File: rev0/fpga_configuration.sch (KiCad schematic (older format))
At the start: 23 parts, among them IC1 ECP5-BGA256, U5 ATSAMD21G18A-AUT, U6 W25Q32JVSS

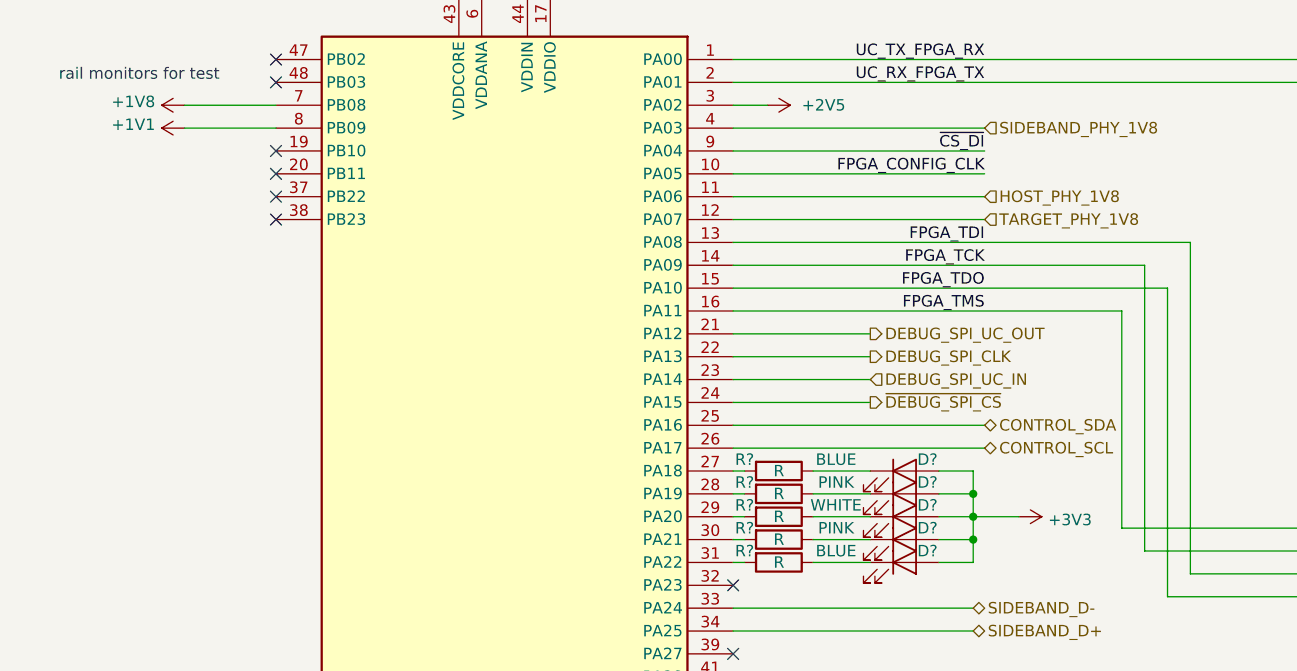
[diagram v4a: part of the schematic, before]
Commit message: schematic: finish initial capture
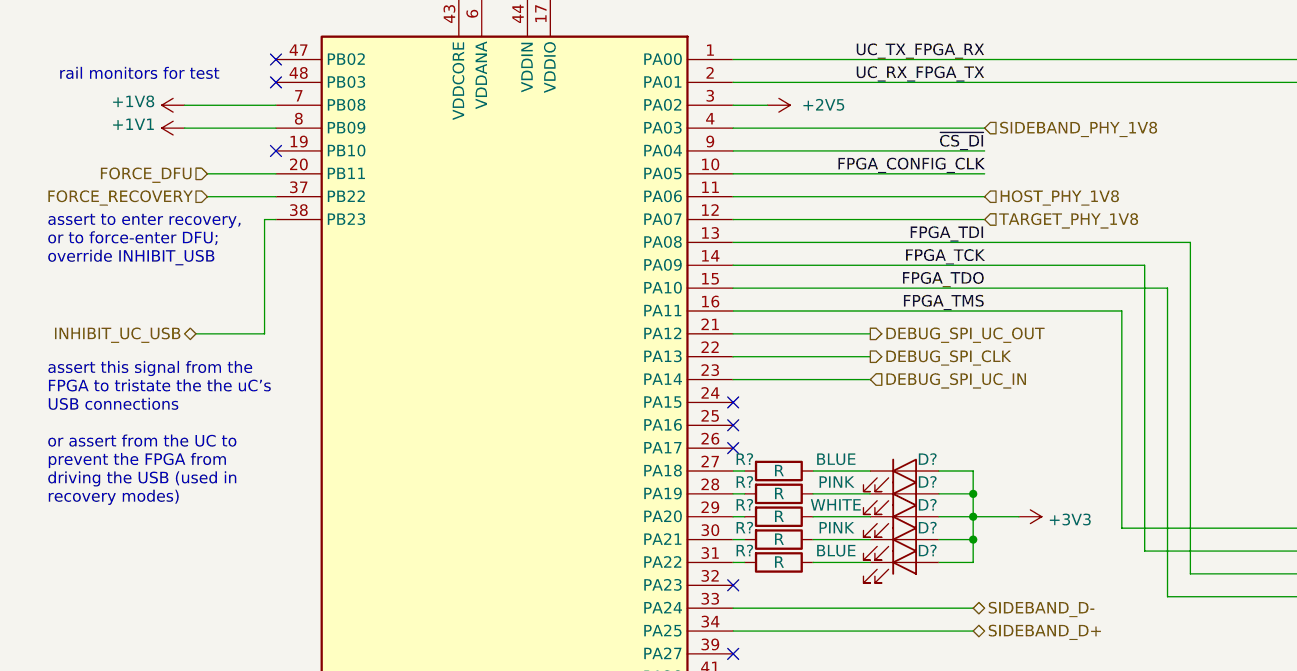
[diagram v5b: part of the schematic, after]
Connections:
- net FORCE_DFU: now reaches U5.20 (PB11)
- net FORCE_RECOVERY: now reaches U5.37 (PB22)
- net INHIBIT_UC_USB: now reaches U5.38 (PB23)
- net CONTROL_SCL: no longer names the net of U5.26 (PA17)
- net CONTROL_SDA: no longer names the net of U5.25 (PA16)
- net ~DEBUG_SPI_CS: no longer names the net of U5.24 (PA15)
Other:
- note added: "assert this signal from the\nFPGA to tristate the the uC’s \nUSB connections\n\nor assert from the UC to\nprevent the FPGA from\ndriving the USB (used in\nrecovery modes)"
- note added: "assert to enter recovery,\nor to force-enter DFU;\noverride INHIBIT_USB"
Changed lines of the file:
@@
 $Descr A4 11693 8268
 encoding utf-8
-Sheet 3 6
-Title "LUNA USB Multitool"
-Date "2019-10-16"
+Sheet 3 9
+Title "LUNA: Configuration / Dev / Debug Section"
+Date "2019-10-20"
 Rev "r0"
 Comp "Great Scott Gadgets"
 Comment1 "Katherine J. Temkin"
 Comment2 ""
-Comment3 ""
+Comment3 "Licensed under the CERN OHL v1.2"
 Comment4 ""
 $EndDescr
@@
 	1    0    0    -1
 $EndComp
-Wire Wire Line
-	2350 1850 2450 1850
-Connection ~ 2450 1850
-Connection ~ 2650 1850
-Wire Wire Line
-	2650 1850 2750 1850
-Wire Wire Line
-	2450 1850 2550 1850
 Connection ~ 2550 1850
-Wire Wire Line
-	2550 1850 2650 1850
 $Comp
 L Device:C C32
@@
 Text Label 8900 4750 2    50   ~ 0
 FPGA_CONFIG_CLK
-$Comp
-L MCU_Microchip_SAMD:ATSAMD21G18A-AUT U5
-U 1 1 5DCDF84F
-P 2550 3750
-F 0 "U5" H 3300 1950 50  0000 C CNN
-F 1 "ATSAMD21G18A-AUT" H 1500 1950 50  0000 C CNN
-F 2 "Package_QFP:TQFP-48_7x7mm_P0.5mm" H 1600 2000 50  0001 C CNN
-F 3 "http://ww1.microchip.com/downloads/en/DeviceDoc/SAMD21-Family-DataSheet-DS40001882D.pdf" H 2550 4750 50  0001 C CNN
-	1    2550 3750
-	-1   0    0    -1
-$EndComp
 Text Label 8900 4200 2    50   ~ 0
 TMS
@@
 UC_SWDIO
 Wire Wire Line
-	3550 3750 4650 3750
-Wire Wire Line
-	3550 3850 4650 3850
-Wire Wire Line
 	5350 4300 5350 3050
 Wire Wire Line
@@
 	3900 4350 4150 4350
 NoConn ~ 3550 4450
-Text HLabel 4650 3750 2    50   BiDi ~ 0
-CONTROL_SDA
-Text HLabel 4650 3850 2    50   BiDi ~ 0
-CONTROL_SCL
 Text HLabel 4150 3350 2    50   Output ~ 0
 DEBUG_SPI_UC_OUT
@@
 Wire Wire Line
 	4150 3550 3550 3550
-Text HLabel 4150 3650 2    50   Output ~ 0
-~DEBUG_SPI_CS
-Wire Wire Line
-	4150 3650 3550 3650
 Text Label 4650 2150 2    50   ~ 0
 UC_TX_FPGA_RX
@@
 NoConn ~ 1550 2250
 NoConn ~ 1550 2550
-NoConn ~ 1550 2650
-NoConn ~ 1550 2750
-NoConn ~ 1550 2850
 Text HLabel 4650 2450 2    50   Input ~ 0
 SIDEBAND_PHY_1V8
@@
 Wire Wire Line
 	1750 5950 1750 6050
+NoConn ~ 3550 3750
+NoConn ~ 3550 3850
+NoConn ~ 3550 3650
+Wire Wire Line
+	2450 1850 2550 1850
+Wire Wire Line
+	2350 1850 2450 1850
+Connection ~ 2450 1850
+Wire Wire Line
+	2550 1850 2650 1850
+Wire Wire Line
+	2650 1850 2750 1850
+Connection ~ 2650 1850
+$Comp
+L MCU_Microchip_SAMD:ATSAMD21G18A-AUT U5
+U 1 1 5DCDF84F
+P 2550 3750
+F 0 "U5" H 3300 1950 50  0000 C CNN
+F 1 "ATSAMD21G18A-AUT" H 1500 1950 50  0000 C CNN
+F 2 "Package_QFP:TQFP-48_7x7mm_P0.5mm" H 1600 2000 50  0001 C CNN
+F 3 "http://ww1.microchip.com/downloads/en/DeviceDoc/SAMD21-Family-DataSheet-DS40001882D.pdf" H 2550 4750 50  0001 C CNN
+	1    2550 3750
+	-1   0    0    -1
+$EndComp
+Text HLabel 1200 3350 0    50   BiDi ~ 0
+INHIBIT_UC_USB
+Text Notes 550  4100 0    50   ~ 0
+assert this signal from the\nFPGA to tristate the the uC’s \nUSB connections\n\nor assert from the UC to\nprevent the FPGA from\ndriving the USB (used in\nrecovery modes)
+Text HLabel 1250 2750 0    50   Input ~ 0
+FORCE_RECOVERY
+Wire Wire Line
+	1250 2750 1550 2750
+Text HLabel 1250 2650 0    50   Input ~ 0
+FORCE_DFU
+Wire Wire Line
+	1550 2650 1250 2650
+Text Notes 550  3050 0    50   ~ 0
+assert to enter recovery,\nor to force-enter DFU;\noverride INHIBIT_USB
+Wire Wire Line
+	1500 3350 1500 2850
+Wire Wire Line
+	1500 2850 1550 2850
+Wire Wire Line
+	1200 3350 1500 3350
 $EndSCHEMATC

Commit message: rev0: finish capture and start routing (woo!)
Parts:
- added R25: 10K, Resistor_SMD:R_0402_1005Metric, symbol Device:R
- C31, C32, C33, C34, C35: footprint (none) -> Capacitor_SMD:C_0402_1005Metric
- D10, D11, D12, D13, D14: renamed from D?; footprint (none) -> LED_SMD:LED_0603_1608Metric_Pad1.05x0.95mm_HandSolder
- IC1: footprint BGA256C80P16X16_1400X1400X170 -> luna:lattice_cabga256
- J5, J6: renamed from J?; footprint (none) -> luna:SWD_CONNECTOR_LARGE_BOX
- R10, R11, R7, R8, R9: renamed from R?; value R -> 330; footprint (none) -> Resistor_SMD:R_0402_1005Metric
- R12: renamed from R5; value R -> 10k; footprint (none) -> Resistor_SMD:R_0402_1005Metric
- R13: renamed from R6; value R -> 10k; footprint (none) -> Resistor_SMD:R_0402_1005Metric
- R14: renamed from R7; value R -> 10k; footprint (none) -> Resistor_SMD:R_0402_1005Metric
- renumbered U5 to U6, U6 to U7
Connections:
- net +3V3: now also R25.1
- net FPGA_DONE: now also U6.24 (PA15)
- net ~FPGA_INIT: now also U6.25 (PA16)
- net ~FPGA_PROGRAM: now also U6.26 (PA17)
- net UC_RESET renamed RESET
- net RESET: now also R25.2
- no-connect marks 18 -> 15
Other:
- note added: "replace w/ ATSAMD21G15B \n(smaller flash) in later rev?"
- note removed: "replace w/ ATSAMD21G15B (smaller flash) in later rev"
- moved on the sheet: D10, D11, D12, D13, D14, R10, R11, R7, R8, R9

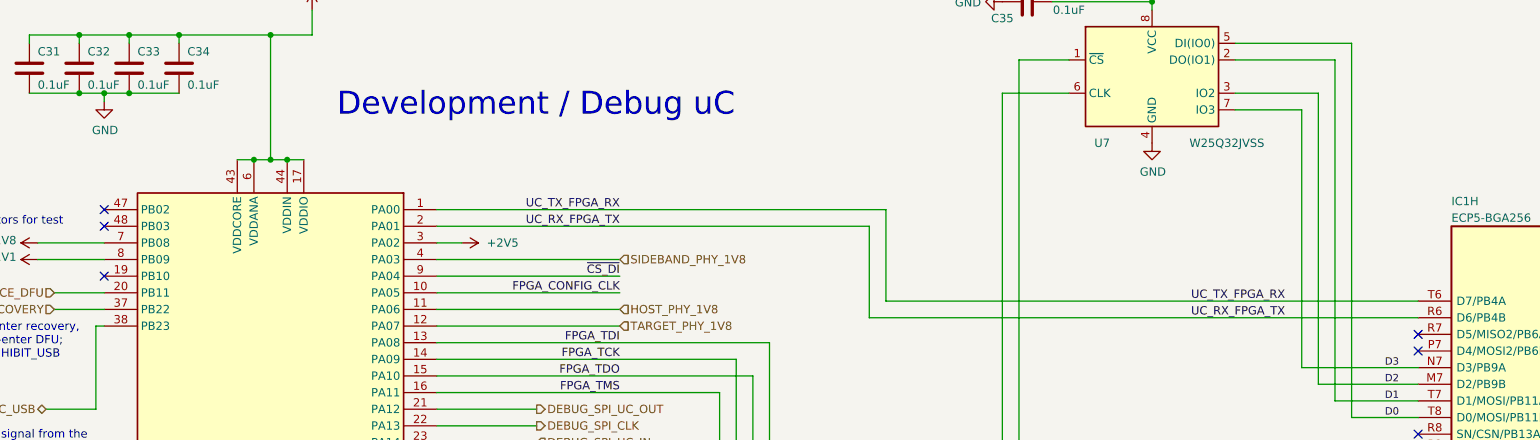
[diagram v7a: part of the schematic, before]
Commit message: rev0: get most of the major routing done
still needs power routing, length matching for the busses,
and routing for the misc control stuff
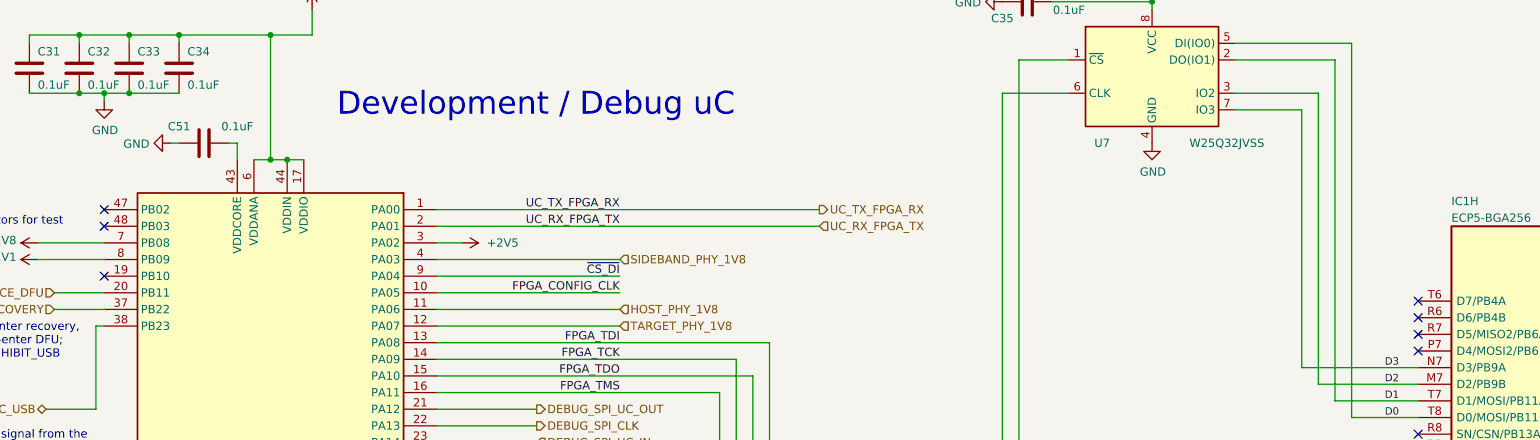
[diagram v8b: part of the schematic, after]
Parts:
- added C51: 0.1uF, Capacitor_SMD:C_0402_1005Metric, symbol Device:C
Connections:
- net +3V3: no longer U6.43 (VDDCORE)
- net GND: now also C51.2
- net UC_RX_FPGA_TX: no longer IC1.R6 (D6/PB4B)
- net UC_TX_FPGA_RX: no longer IC1.T6 (D7/PB4A)
- new net: C51.1, U6.43 (VDDCORE)
- no-connect marks 15 -> 17
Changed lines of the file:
@@
 Text Label 4650 2150 2    50   ~ 0
 UC_TX_FPGA_RX
-Wire Wire Line
-	9450 2700 6250 2700
-Wire Wire Line
-	6250 2700 6250 2150
-Wire Wire Line
-	3550 2150 6250 2150
-Wire Wire Line
-	9450 2800 6150 2800
-Wire Wire Line
-	6150 2800 6150 2250
-Wire Wire Line
-	6150 2250 3550 2250
 Text Label 4650 2250 2    50   ~ 0
-UC_RX_FPGA_TX
-Text Label 8650 2700 2    50   ~ 0
-UC_TX_FPGA_RX
-Text Label 8650 2800 2    50   ~ 0
 UC_RX_FPGA_TX
 Wire Wire Line
@@
 	2450 1850 2550 1850
 Wire Wire Line
-	2350 1850 2450 1850
-Connection ~ 2450 1850
-Wire Wire Line
 	2550 1850 2650 1850
 Wire Wire Line
 	2650 1850 2750 1850
 Connection ~ 2650 1850
+Text HLabel 1250 2750 0    50   Input ~ 0
+FORCE_RECOVERY
+Wire Wire Line
+	1250 2750 1550 2750
+Text HLabel 1250 2650 0    50   Input ~ 0
+FORCE_DFU
+Wire Wire Line
+	1550 2650 1250 2650
+Wire Wire Line
+	1500 3350 1500 2850
+Wire Wire Line
+	1500 2850 1550 2850
+Wire Wire Line
+	1200 3350 1500 3350
+Wire Wire Line
+	5250 4200 9450 4200
+Text Notes 550  3050 0    50   ~ 0
+assert to enter recovery,\nor to force-enter DFU;\noverride INHIBIT_USB
+Text Notes 550  4100 0    50   ~ 0
+assert this signal from the\nFPGA to tristate the the uC’s \nUSB connections\n\nor assert from the UC to\nprevent the FPGA from\ndriving the USB (used in\nrecovery modes)
+Text HLabel 1200 3350 0    50   BiDi ~ 0
+INHIBIT_UC_USB
+$Comp
+L Device:LED D10
+U 1 1 5DB78DC3
+P 4350 3950
+F 0 "D10" H 4500 4000 50  0000 C CNN
+F 1 "BLUE" H 4050 4000 50  0000 C CNN
+F 2 "LED_SMD:LED_0603_1608Metric_Pad1.05x0.95mm_HandSolder" H 4350 3950 50  0001 C CNN
+F 3 "~" H 4350 3950 50  0001 C CNN
+	1    4350 3950
+	1    0    0    1
+$EndComp
+Wire Wire Line
+	3550 4250 3650 4250
+Wire Wire Line
+	3550 4350 3650 4350
+Wire Wire Line
+	3550 4150 3650 4150
+Wire Wire Line
+	3550 4050 3650 4050
+Wire Wire Line
+	3550 3950 3650 3950
+$Comp
+L Device:R R25
+U 1 1 5E28BD64
+P 5450 5000
+F 0 "R25" H 5520 5045 50  0000 L CNN
+F 1 "10K" V 5450 4950 50  0000 L CNN
+F 2 "Resistor_SMD:R_0402_1005Metric" V 5380 5000 50  0001 C CNN
+F 3 "~" H 5450 5000 50  0001 C CNN
+	1    5450 5000
+	1    0    0    -1
+$EndComp
+Wire Wire Line
+	5150 5250 5450 5250
+Connection ~ 5150 5250
+Wire Wire Line
+	5450 5150 5450 5250
+$Comp
+L power:+3V3 #PWR0103
+U 1 1 5E29AB77
+P 5450 4850
+F 0 "#PWR0103" H 5450 4700 50  0001 C CNN
+F 1 "+3V3" H 5464 5023 50  0000 C CNN
+F 2 "" H 5450 4850 50  0001 C CNN
+F 3 "" H 5450 4850 50  0001 C CNN
+	1    5450 4850
+	1    0    0    -1
+$EndComp
+Connection ~ 5450 5250
+Wire Wire Line
+	5450 5250 5700 5250
+Text HLabel 5700 5250 2    50   Input ~ 0
+RESET
+Wire Wire Line
+	4150 3350 3550 3350
+Wire Wire Line
+	3550 3650 4150 3650
+Wire Wire Line
+	3550 3750 4150 3750
+Wire Wire Line
+	3550 3850 4150 3850
+Text Label 4150 3650 2    50   ~ 0
+FPGA_DONE
+Text Label 4150 3750 2    50   ~ 0
+~FPGA_INIT
+Text Label 4150 3850 2    50   ~ 0
+~FPGA_PROGRAM
 $Comp
 L MCU_Microchip_SAMD:ATSAMD21G18A-AUT U6
@@
 	-1   0    0    -1
 $EndComp
-Text HLabel 1250 2750 0    50   Input ~ 0
-FORCE_RECOVERY
-Wire Wire Line
-	1250 2750 1550 2750
-Text HLabel 1250 2650 0    50   Input ~ 0
-FORCE_DFU
-Wire Wire Line
-	1550 2650 1250 2650
-Wire Wire Line
-	1500 3350 1500 2850
-Wire Wire Line
-	1500 2850 1550 2850
-Wire Wire Line
-	1200 3350 1500 3350
-Wire Wire Line
-	5250 4200 9450 4200
-Text Notes 550  3050 0    50   ~ 0
-assert to enter recovery,\nor to force-enter DFU;\noverride INHIBIT_USB
-Text Notes 550  4100 0    50   ~ 0
-assert this signal from the\nFPGA to tristate the the uC’s \nUSB connections\n\nor assert from the UC to\nprevent the FPGA from\ndriving the USB (used in\nrecovery modes)
-Text HLabel 1200 3350 0    50   BiDi ~ 0
-INHIBIT_UC_USB
-$Comp
-L Device:LED D10
-U 1 1 5DB78DC3
-P 4350 3950
-F 0 "D10" H 4500 4000 50  0000 C CNN
-F 1 "BLUE" H 4050 4000 50  0000 C CNN
-F 2 "LED_SMD:LED_0603_1608Metric_Pad1.05x0.95mm_HandSolder" H 4350 3950 50  0001 C CNN
-F 3 "~" H 4350 3950 50  0001 C CNN
-	1    4350 3950
-	1    0    0    1
-$EndComp
-Wire Wire Line
-	3550 4250 3650 4250
-Wire Wire Line
-	3550 4350 3650 4350
-Wire Wire Line
-	3550 4150 3650 4150
-Wire Wire Line
-	3550 4050 3650 4050
-Wire Wire Line
-	3550 3950 3650 3950
-$Comp
-L Device:R R25
-U 1 1 5E28BD64
-P 5450 5000
-F 0 "R25" H 5520 5045 50  0000 L CNN
-F 1 "10K" V 5450 4950 50  0000 L CNN
-F 2 "Resistor_SMD:R_0402_1005Metric" V 5380 5000 50  0001 C CNN
-F 3 "~" H 5450 5000 50  0001 C CNN
-	1    5450 5000
-	1    0    0    -1
-$EndComp
-Wire Wire Line
-	5150 5250 5450 5250
-Connection ~ 5150 5250
-Wire Wire Line
-	5450 5150 5450 5250
-$Comp
-L power:+3V3 #PWR0103
-U 1 1 5E29AB77
-P 5450 4850
-F 0 "#PWR0103" H 5450 4700 50  0001 C CNN
-F 1 "+3V3" H 5464 5023 50  0000 C CNN
-F 2 "" H 5450 4850 50  0001 C CNN
-F 3 "" H 5450 4850 50  0001 C CNN
-	1    5450 4850
-	1    0    0    -1
-$EndComp
-Connection ~ 5450 5250
-Wire Wire Line
-	5450 5250 5700 5250
-Text HLabel 5700 5250 2    50   Input ~ 0
-RESET
-Wire Wire Line
-	4150 3350 3550 3350
-Wire Wire Line
-	3550 3650 4150 3650
-Wire Wire Line
-	3550 3750 4150 3750
-Wire Wire Line
-	3550 3850 4150 3850
-Text Label 4150 3650 2    50   ~ 0
-FPGA_DONE
-Text Label 4150 3750 2    50   ~ 0
-~FPGA_INIT
-Text Label 4150 3850 2    50   ~ 0
-~FPGA_PROGRAM
+Wire Wire Line
+	2350 1850 2350 1750
+$Comp
+L Device:C C51
+U 1 1 5E10AFD4
+P 2150 1750
+F 0 "C51" V 2050 1600 50  0000 C CNN
+F 1 "0.1uF" V 2050 1950 50  0000 C CNN
+F 2 "Capacitor_SMD:C_0402_1005Metric" H 2188 1600 50  0001 C CNN
+F 3 "~" H 2150 1750 50  0001 C CNN
+	1    2150 1750
+	0    1    1    0
+$EndComp
+Wire Wire Line
+	2300 1750 2350 1750
+$Comp
+L power:GND #PWR0112
+U 1 1 5E121F7E
+P 1950 1750
+F 0 "#PWR0112" H 1950 1500 50  0001 C CNN
+F 1 "GND" V 1955 1622 50  0000 R CNN
+F 2 "" H 1950 1750 50  0001 C CNN
+F 3 "" H 1950 1750 50  0001 C CNN
+	1    1950 1750
+	0    1    1    0
+$EndComp
+Wire Wire Line
+	1950 1750 2000 1750
+Text HLabel 5850 2150 2    50   Output ~ 0
+UC_TX_FPGA_RX
+Wire Wire Line
+	3550 2150 5850 2150
+Text HLabel 5850 2250 2    50   Input ~ 0
+UC_RX_FPGA_TX
+Wire Wire Line
+	5850 2250 3550 2250
+NoConn ~ 9450 2700
+NoConn ~ 9450 2800
 $EndSCHEMATC
